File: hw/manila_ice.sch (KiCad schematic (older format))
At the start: 12 parts, among them J1 USB_B

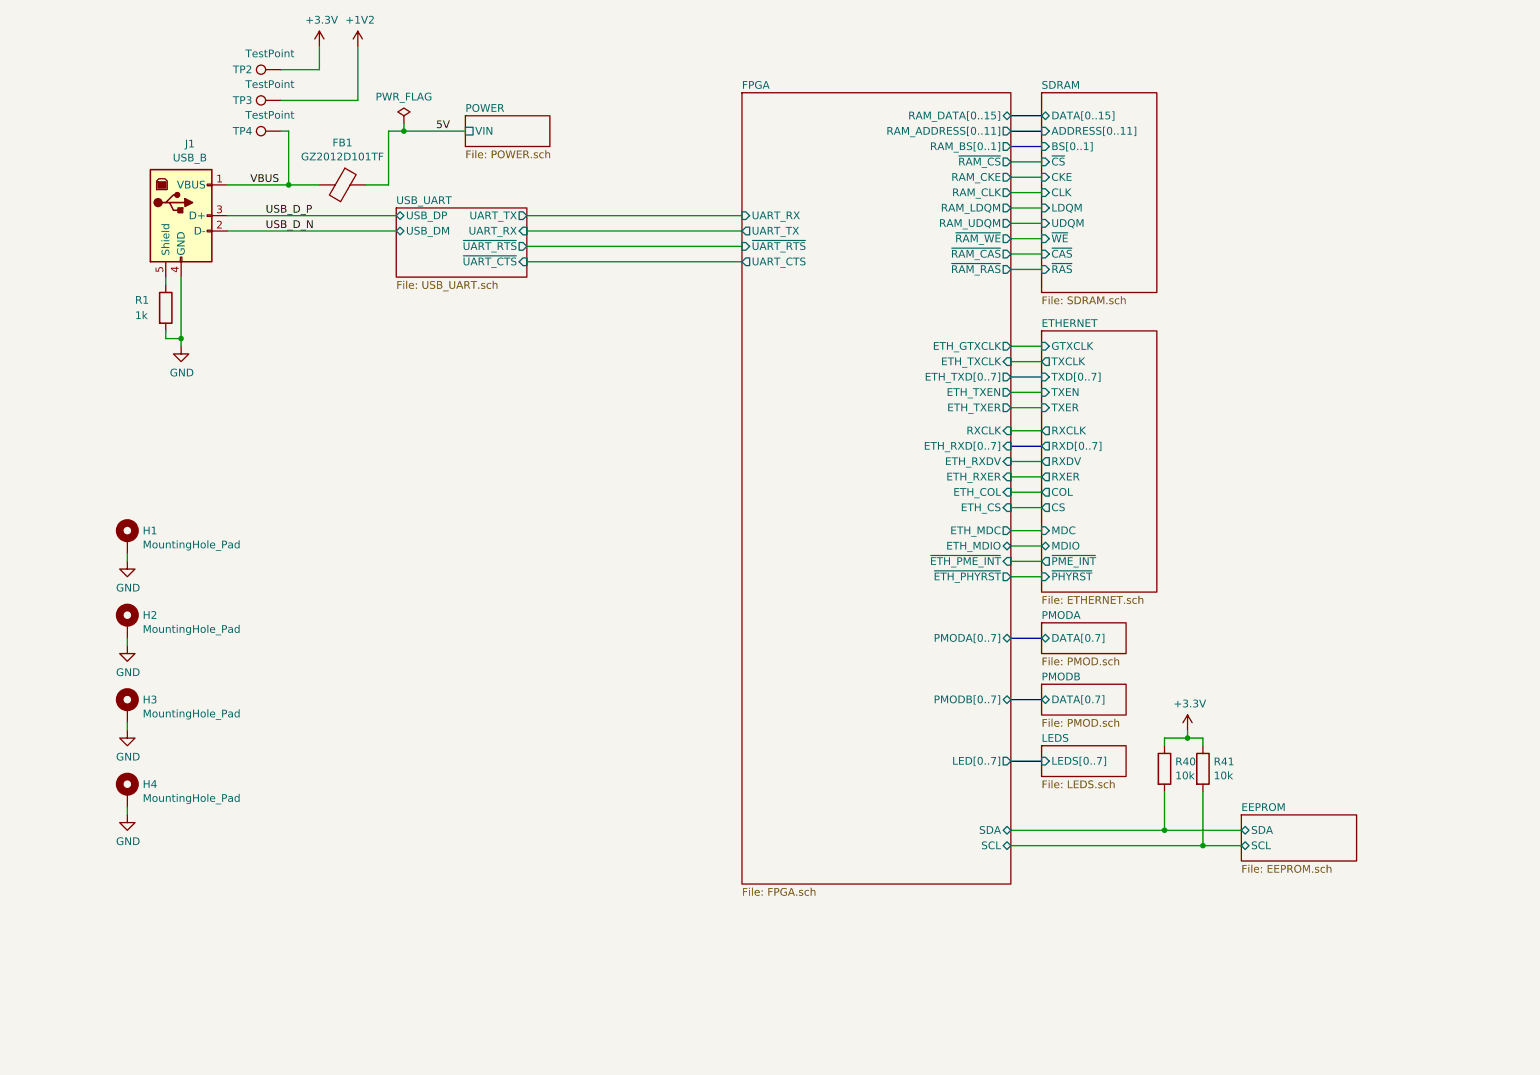
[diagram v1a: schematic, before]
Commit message: Move to switched mode regulators. Layout not complete yet
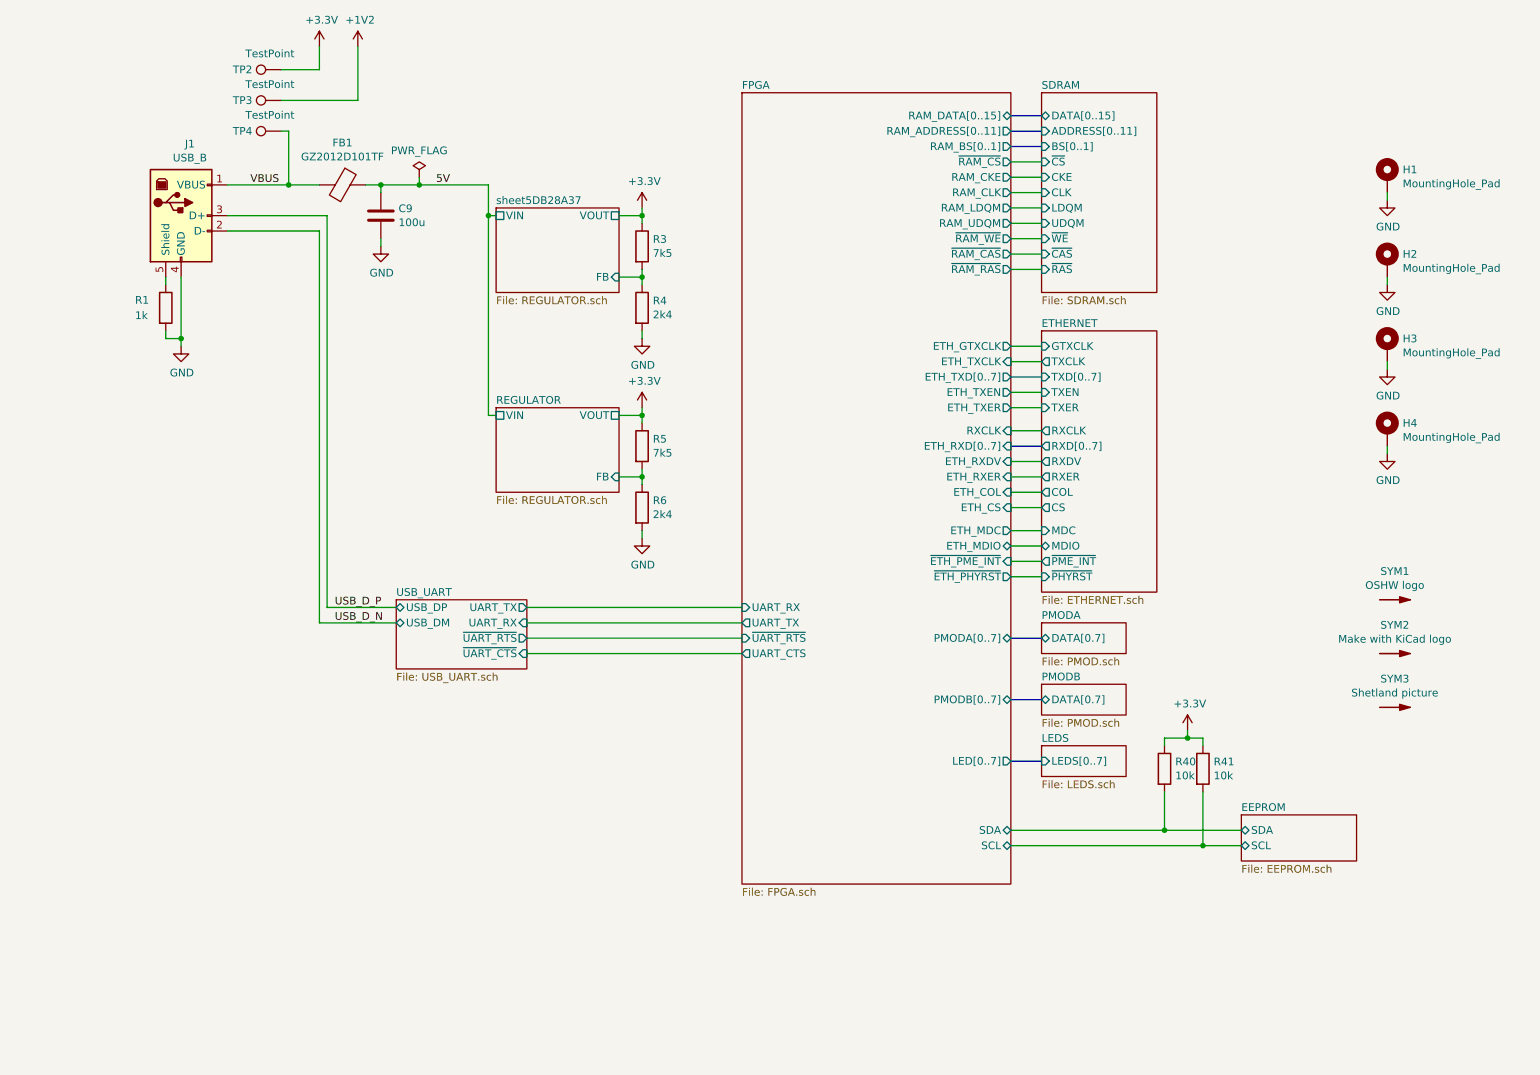
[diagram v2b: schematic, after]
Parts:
- added C9: 100u, Capacitor_Tantalum_SMD:CP_EIA-3216-18_Kemet-A, symbol Device:C
- added R3, R5: 7k5, Resistor_SMD:R_0603_1608Metric, symbol Device:R
- added R4, R6: 2k4, Resistor_SMD:R_0603_1608Metric, symbol Device:R
- added SYM1: OSHW logo, Symbol:OSHW-Logo_5.7x6mm_SilkScreen, symbol Graphic:SYM_Arrow_Normal
- added SYM2: Make with KiCad logo, Symbol:KiCad-Logo2_5mm_SilkScreen, symbol Graphic:SYM_Arrow_Normal
- added SYM3: Shetland picture, Art:Shetland_combined, symbol Graphic:SYM_Arrow_Normal
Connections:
- net +3V3: now also R3.1, R5.1
- net 5V: now also C9.1
- net GND: now also C9.2, R4.2, R6.2
- new net REGULATOR/FB: R5.2, R6.1
- new net sheet5DB28A37/FB: R3.2, R4.1
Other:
- moved on the sheet: H1, H2, H3, H4

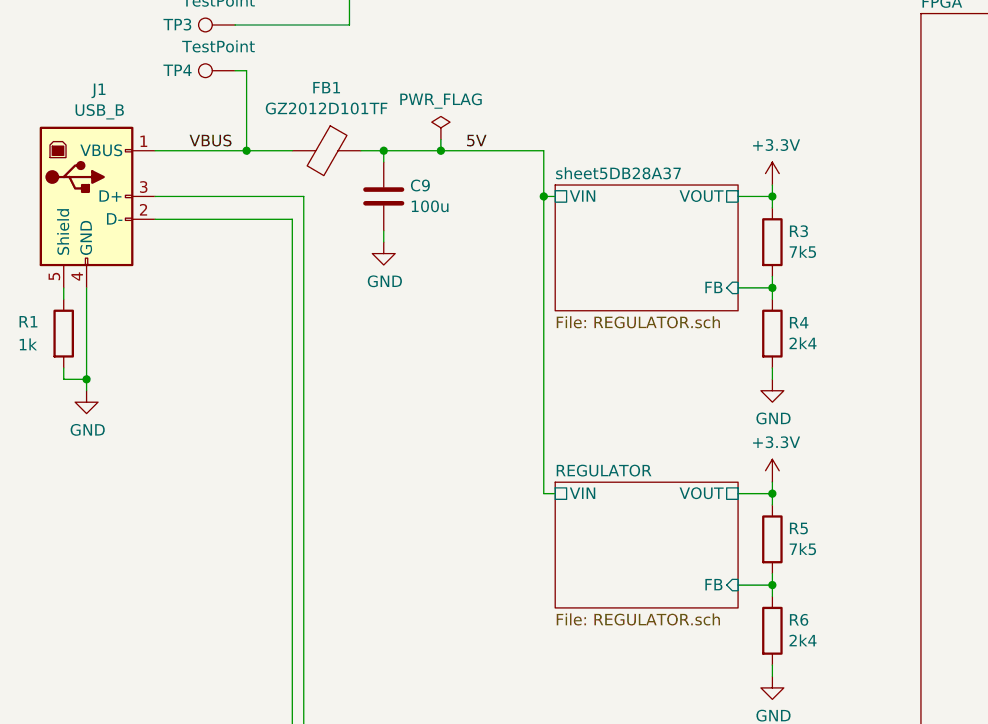
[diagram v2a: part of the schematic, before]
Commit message: Plumbed in SMPS
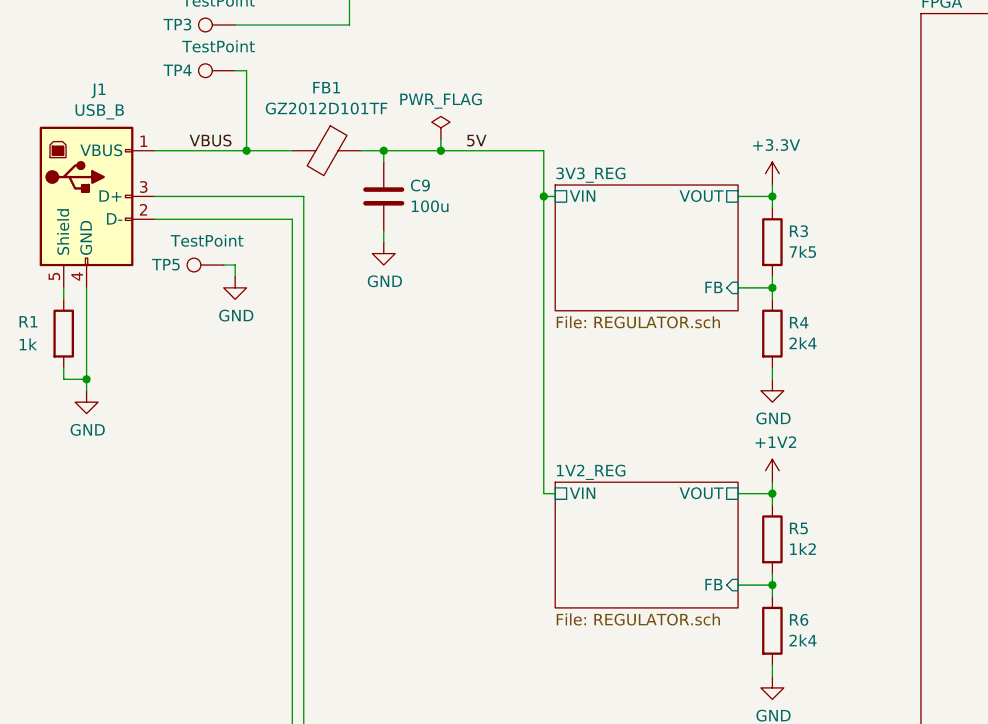
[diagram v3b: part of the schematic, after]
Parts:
- added TP5: TestPoint, TestPoint:TestPoint_Pad_D1.0mm, symbol Connector:TestPoint
- R5: value 7k5 -> 1k2
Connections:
- net +1V2: now also R5.1
- net +3V3: no longer R5.1
- net GND: now also TP5.1
- net REGULATOR/FB renamed 1V2_REG/FB
- net sheet5DB28A37/FB renamed 3V3_REG/FB
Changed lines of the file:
@@
 S 3650 3050 800  550
 U 5DAFE486
-F0 "REGULATOR" 50
+F0 "1V2_REG" 50
 F1 "REGULATOR.sch" 50
 F2 "FB" I R 4450 3500 50
@@
 P 4600 3300
 F 0 "R5" H 4670 3346 50  0000 L CNN
-F 1 "7k5" H 4670 3255 50  0000 L CNN
+F 1 "1k2" H 4670 3255 50  0000 L CNN
 F 2 "Resistor_SMD:R_0603_1608Metric" V 4530 3300 50  0001 C CNN
 F 3 "~" H 4600 3300 50  0001 C CNN
@@
 Wire Wire Line
 	2900 1650 2900 1600
-$Comp
-L power:+3.3V #PWR025
-U 1 1 5DB14C3C
-P 4600 3050
-AR Path="/5DB14C3C" Ref="#PWR025"  Part="1"
-AR Path="/5D7E2E67/5DB14C3C" Ref="#PWR?"  Part="1"
-F 0 "#PWR025" H 4600 2900 50  0001 C CNN
-F 1 "+3.3V" H 4615 3223 50  0000 C CNN
-F 2 "" H 4600 3050 50  0001 C CNN
-F 3 "" H 4600 3050 50  0001 C CNN
-	1    4600 3050
-	1    0    0    -1
-$EndComp
 Wire Wire Line
 	4450 3100 4600 3100
@@
 S 3650 1750 800  550
 U 5DB28A3C
-F0 "sheet5DB28A37" 50
+F0 "3V3_REG" 50
 F1 "REGULATOR.sch" 50
 F2 "FB" I R 4450 2200 50
@@
 	1    0    0    -1
 $EndComp
+$Comp
+L power:+1V2 #PWR?
+U 1 1 5DB0C35C
+P 4600 3050
+AR Path="/5D7E2E67/5DB0C35C" Ref="#PWR?"  Part="1"
+AR Path="/5DB0C35C" Ref="#PWR0148"  Part="1"
+F 0 "#PWR0148" H 4600 2900 50  0001 C CNN
+F 1 "+1V2" H 4615 3223 50  0000 C CNN
+F 2 "" H 4600 3050 50  0001 C CNN
+F 3 "" H 4600 3050 50  0001 C CNN
+	1    4600 3050
+	1    0    0    -1
+$EndComp
+$Comp
+L Connector:TestPoint TP?
+U 1 1 5DB80F95
+P 2200 2100
+AR Path="/5E257EC5/5DB80F95" Ref="TP?"  Part="1"
+AR Path="/5DB80F95" Ref="TP5"  Part="1"
+F 0 "TP5" V 2200 2350 50  0000 C CNN
+F 1 "TestPoint" V 2304 2172 50  0000 C CNN
+F 2 "TestPoint:TestPoint_Pad_D1.0mm" H 2400 2100 50  0001 C CNN
+F 3 "~" H 2400 2100 50  0001 C CNN
+F 4 "0" H 2200 2450 50  0001 C CNN "JLCPCB BOM"
+	1    2200 2100
+	0    -1   -1   0
+$EndComp
+$Comp
+L power:GND #PWR025
+U 1 1 5DB81941
+P 2250 2150
+F 0 "#PWR025" H 2250 1900 50  0001 C CNN
+F 1 "GND" H 2255 1977 50  0000 C CNN
+F 2 "" H 2250 2150 50  0001 C CNN
+F 3 "" H 2250 2150 50  0001 C CNN
+	1    2250 2150
+	1    0    0    -1
+$EndComp
+Wire Wire Line
+	2200 2100 2250 2100
+Wire Wire Line
+	2250 2100 2250 2150
 $EndSCHEMATC

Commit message: Fixed tant footprint. Added JLC part numbers to other components
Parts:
- C9: footprint Capacitor_Tantalum_SMD:CP_EIA-3216-18_Kemet-A -> Capacitor_Tantalum_SMD:CP_EIA-3528-21_Kemet-B; LCSC Part (none) -> C16133
- R3: LCSC Part (none) -> C22452
- R4, R6: LCSC Part (none) -> C22940
- R5: LCSC Part (none) -> C22765
- SYM1, SYM2, SYM3: JLCPCB BOM (none) -> 0

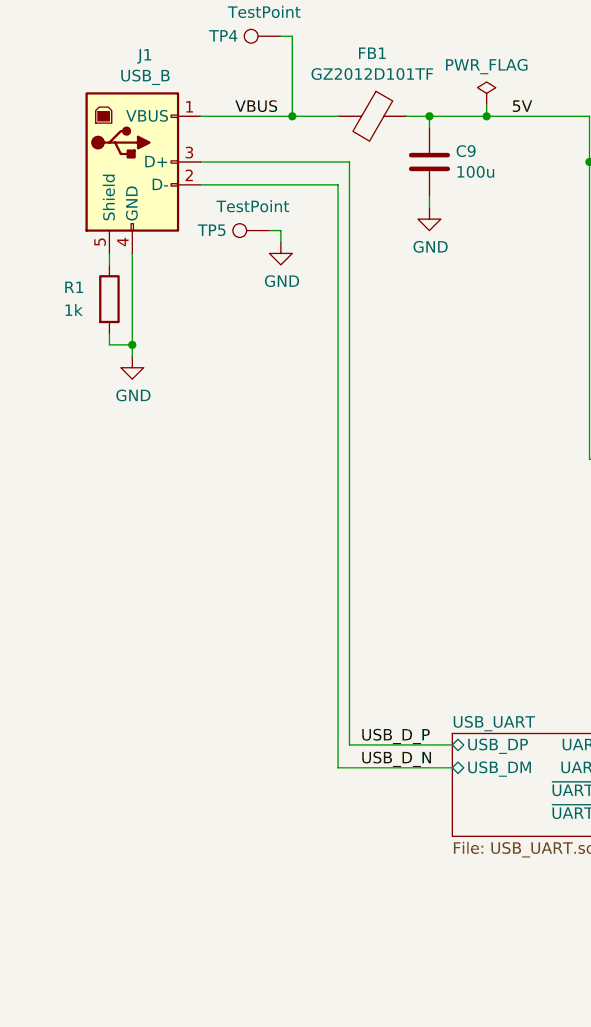
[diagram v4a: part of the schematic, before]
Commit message: Add ESD protection
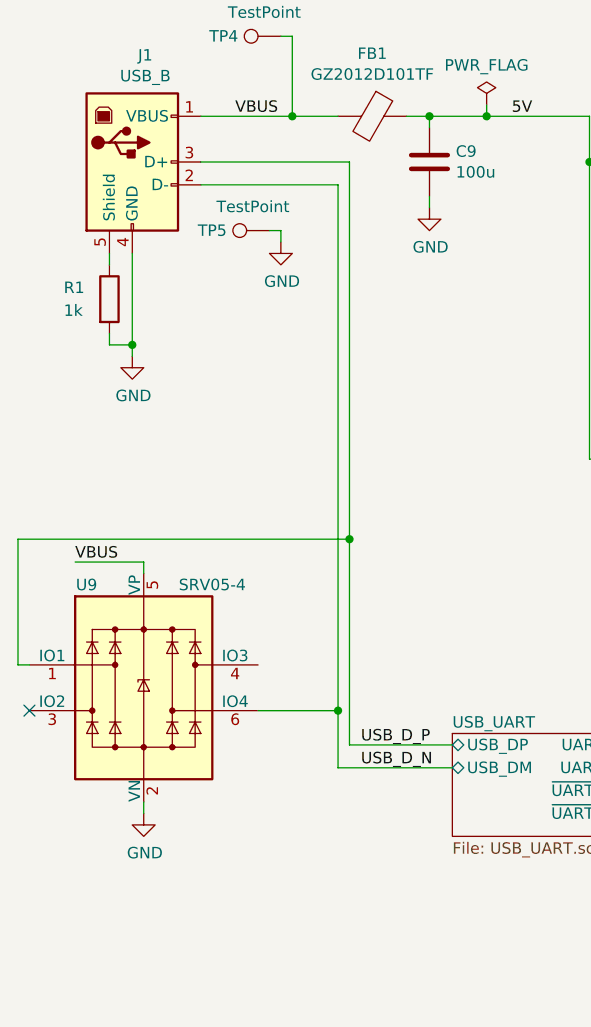
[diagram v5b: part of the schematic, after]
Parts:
- added U9: SRV05-4, Package_TO_SOT_SMD:SOT-23-6, symbol Power_Protection:SRV05-4
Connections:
- net GND: now also U9.2 (VN)
- net USB_D_N: now also U9.6 (IO4)
- net USB_D_P: now also U9.1 (IO1)
- net VBUS: now also U9.5 (VP)
- no-connect marks 0 -> 1

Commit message: Fix JLC rotation
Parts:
- C9: symbol Device:C -> Device:CP; JLCPCB Rotation (none) -> 180
- FB1, R1, R4, R40, R41, R5, R6: JLCPCB Rotation (none) -> 0
- R3: JLCPCB Rotation (none) -> 0; LCSC Part C22452 -> C23234
- U9: JLCPCB Rotation (none) -> 180
